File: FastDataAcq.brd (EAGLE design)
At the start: 160 x 100 mm, 229 parts, among them IC1 LT1963AEQ, IC2 FT230XQ, IC3 ADCMP553BRMZ, J1 USB_MICROAB_SMT, J2 MICRO-FIT_3.0_2POS_RA_SMD, X1 SMA-142-0701-801/806, X2 87832-14, X3 SMA-142-0701-801/806, Y1 SI530-500, Y2 DNP, Y3 100MHz

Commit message: Schematic fixes and beginning board layout
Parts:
- removed C105, C106, C107, C108, C109, C110, C111, C112: .1uF, Schuyler:0204REVERSE
- removed R40: 100 0.1%, rcl:R0402
- removed R41: 330, rcl:R0201
- added C16: .1uF, Schuyler:0204REVERSE
- added C66: 10pF, rcl:C0201
- added C67: 33uF, SparkFun-Passives:0805
- added C69, C73: 22uF 150mOhm ESR, rcl:C0805
- added C70, C72: 10uF, rcl:C0603
- added C75: NA, rcl:C0603
- C10, C11, C28, C29, C87: value 33uF -> .1uF; device SparkFun-Passives:0805 -> Schuyler:0204REVERSE
- C100: value .1uF -> 47pF; device Schuyler:0204REVERSE -> rcl:C0201
- C101, C103: value .1uF -> 10nF; device Schuyler:0204REVERSE -> rcl:C0201
- C102: value 4.7uF -> 1uF; device Schuyler:0306REVERSE -> Schuyler:0204REVERSE
- C12, C13, C15, C17, C22: value 10uF -> .1uF; device rcl:C0603 -> Schuyler:0204REVERSE
- C14, C25, C26, C27, C8, C9: value 10pF -> .1uF; device rcl:C0201 -> Schuyler:0204REVERSE
- C18: value NA -> 10uF
- C2: value 10uF -> 10pF; device rcl:C0603 -> rcl:C0201
- C20: value 10uF -> 100uF; device rcl:C0603 -> Schuyler:2917_MURATA_CAP
- C23, C24: value 22uF 150mOhm ESR -> .1uF; device rcl:C0805 -> Schuyler:0204REVERSE
- C3: value 100uF -> 33uF; device Schuyler:2917_MURATA_CAP -> SparkFun-Passives:0805
- C30, C38: value 33uF -> 0.47uF; device SparkFun-Passives:0805 -> Schuyler:0204REVERSE
- C31: value 22uF 150mOhm ESR -> 33uF; device rcl:C0805 -> SparkFun-Passives:0805
- C32, C65, C68: value 4.7uF -> 10uF; device Schuyler:0306REVERSE -> rcl:C0603
- C33, C71: value 4.7uF -> 10pF; device Schuyler:0306REVERSE -> rcl:C0201
- C34, C74: value 4.7uF -> 33uF; device Schuyler:0306REVERSE -> SparkFun-Passives:0805
- C35, C40, C50: device Schuyler:0306REVERSE -> Schuyler:0402_C
- C36, C37, C41, C42, C45, C62: value 0.47uF -> 4.7uF; device Schuyler:0306REVERSE -> Schuyler:0402_C
- C39: value 33uF -> 4.7uF; device SparkFun-Passives:0805 -> Schuyler:0402_C
- C43, C44, C47, C93: value .1uF -> 4.7uF; device Schuyler:0204REVERSE -> Schuyler:0402_C
- C46, C48, C49: value .1uF -> 0.47uF
- C5: value NA -> 10pF; device rcl:C0603 -> rcl:C0201
- C51, C52, C60: value 4.7uF -> 0.47uF; device Schuyler:0306REVERSE -> Schuyler:0204REVERSE
- C53, C58: value .1uF -> 10uF; device Schuyler:0204REVERSE -> rcl:C0603
- C54: value .1uF -> 10pF; device Schuyler:0204REVERSE -> rcl:C0201
- C55: value 0.47uF -> 33uF; device Schuyler:0306REVERSE -> SparkFun-Passives:0805
- C56: value 0.47uF -> 10uF; device Schuyler:0306REVERSE -> rcl:C0603
- C57: value 4.7uF -> 22uF 150mOhm ESR; device Schuyler:0306REVERSE -> rcl:C0805
- C59: value 10nF -> 4.7uF; device rcl:C0201 -> Schuyler:0402_C
- C6: value 10uF -> 33uF; device rcl:C0603 -> SparkFun-Passives:0805
- C61: device Schuyler:0306REVERSE -> Schuyler:0204REVERSE
- C63: value 1uF -> 0.47uF
- C64: value 10nF -> 0.47uF; device rcl:C0201 -> Schuyler:0204REVERSE
- C7: value 10uF -> NA
- C76: value 0.47uF -> 10nF; device Schuyler:0306REVERSE -> rcl:C0201
- C77: value 100pF -> .1uF; device rcl:C0603 -> Schuyler:0204REVERSE
- C78: value .1uF -> 1uF
- C79, C82: value .1uF -> 4.7nF; device Schuyler:0204REVERSE -> rcl:C0201
- C80: value 4.7nF -> .1uF; device rcl:C0201 -> Schuyler:0204REVERSE
- C81: value 4.7nF -> 1uF; device rcl:C0201 -> Schuyler:0204REVERSE
- C84: value 33uF -> 10nF; device SparkFun-Passives:0805 -> rcl:C0201
- C86: value 1uF -> 10nF; device Schuyler:0204REVERSE -> rcl:C0201
- C88: value 4.7uF -> 100pF; device Schuyler:0306REVERSE -> rcl:C0201
- C90, C94: value 10nF -> .1uF; device rcl:C0201 -> Schuyler:0204REVERSE
- C91: value .1uF -> 33uF; device Schuyler:0204REVERSE -> SparkFun-Passives:0805
- C92: value 10nF -> 4.7uF; device rcl:C0201 -> Schuyler:0306REVERSE
- C96: value 47pF -> .1uF; device rcl:C0201 -> Schuyler:0204REVERSE
- C98: value 47pF -> 33uF; device rcl:C0201 -> SparkFun-Passives:0805
- C99: value 1uF -> 47pF; device Schuyler:0204REVERSE -> rcl:C0201
- J1: value USB_MICROAB_SMT -> MICRO-FIT_3.0_2POS_RA_SMD; device Schuyler:USB_MICROAB_SMT_1 -> Schuyler:MICRO-FIT_3.02POS_RA_SMD
- J2: value MICRO-FIT_3.0_2POS_RA_SMD -> USB_MICROAB_SMT; device Schuyler:MICRO-FIT_3.02POS_RA_SMD -> Schuyler:USB_MICROAB_SMT_1
- JP2: value M10" -> (none); device SparkFun-Connectors:1X10 -> SparkFun-Passives:1X02
- JP3: value (none) -> M10"; device SparkFun-Passives:1X02 -> SparkFun-Connectors:1X10
- L10, L7, L9: value (none) -> 2.2uH; device Schuyler:MURATA_BLM18 -> Schuyler:3.0X3.6_VISHAY
- L12: value CHOKE_CM_ACM7060-301 -> (none); device Schuyler:ACM7060_CHOKE -> Schuyler:MURATA_BLM18
- L2: value 2.2uH -> CHOKE_CM_ACM7060-301; device Schuyler:3.0X3.6_VISHAY -> Schuyler:ACM7060_CHOKE
- L4, L5: value 2.2uH -> (none); device Schuyler:3.0X3.6_VISHAY -> Schuyler:MURATA_BLM18
- L6: value 2.2uH -> (none); device Schuyler:5.18X5.49_VISHAY -> Schuyler:MURATA_BLM18
- L8: value (none) -> 2.2uH; device Schuyler:MURATA_BLM18 -> Schuyler:5.18X5.49_VISHAY
- R1, R6: value NA -> 10k; device rcl:R0603 -> rcl:R0201
- R10: value NA -> 210K; device rcl:R0603 -> rcl:R0201
- R11: value 649K -> 422K
- R12: value 150K -> 10k
- R13: value NA -> 270k; device rcl:R0603 -> rcl:R0201
- R14: value 523K -> 1k
- R15: value 523K -> 845k
- R16: value 523K -> 210K
- R17: value 210K -> 270k
- R18: value 150K -> 523K
- R19: value 523K -> 806K
- R20: value 280K -> 649K
- R21: value 270k -> 523K
- R22: value 210K -> 1.15k 1%; device rcl:R0201 -> rcl:R0603
- R23, R34, R4, R8: value 10k -> NA; device rcl:R0201 -> rcl:R0603
- R24: value 1k -> 280K
- R25: value 210K -> 100; device rcl:R0201 -> rcl:R0603
- R26: value 806K -> 2k 1%; device rcl:R0201 -> rcl:R0603
- R27: value 845k -> 523K
- R28: value 649K -> NA; device rcl:R0201 -> rcl:R0603
- R29: value 422K -> 210K
- R30: value 270k -> 649K
- R31: value 1.15k 1% -> 523K; device rcl:R0603 -> rcl:R0201
- R32: value 2k 1% -> 150K; device rcl:R0603 -> rcl:R0201
- R33: value 50 -> 150K
- R35, R36: value 10k -> 100 0.1%; device rcl:R0201 -> rcl:R0402
- R37: value 10k -> 4.7k
- R38: value NA -> 330; device rcl:R0603 -> rcl:R0201
- R39: value 100 0.1% -> 0; device rcl:R0402 -> rcl:R0603
- R42: value 4.7k -> 330
- R43: value 0 -> 330; device rcl:R0603 -> rcl:R0201
- R46, R47: value 27 -> 330
- R48: value 10k -> 330; device rcl:R0603 -> rcl:R0201
- R49: value 26.1k -> 10k; device rcl:R0603 -> rcl:R0201
- R50: device rcl:R0603 -> rcl:R0201
- R51: value 16k -> 50; device rcl:R0603 -> rcl:R0201
- R52, R53: value 50 -> 27
- R54: value 50 -> 26.1k; device rcl:R0201 -> rcl:R0603
- R55: value 100 -> 16k
- R56, R57: value 330 -> 10k; device rcl:R0201 -> rcl:R0603
- R58: value 330 -> NA; device rcl:R0201 -> rcl:R0603
- R59, R60: value 330 -> 50
- R62: value NA -> 50; device rcl:R0603 -> rcl:R0201
- R7: value 3.3k 0.1% -> 4.7k; device rcl:R0603 -> rcl:R0201
- R9: value 4.7k -> 3.3k 0.1%; device rcl:R0201 -> rcl:R0603
- U$10: value XCFXXS04 -> LMH6555; device Schuyler:TSSOP20_XILINX -> Schuyler:16WQFN
- U$11: value SLIDER_SPDT_1101M2S3AQE2 -> LMV321SC-70; device Schuyler:C_AND_K_1101M2S3AQE2 -> Schuyler:SC-70
- U$3: value LTC3374QFN -> SLIDER_SPDT_1101M2S3AQE2; device Schuyler:38-QFN_(5X7) -> Schuyler:C_AND_K_1101M2S3AQE2
- U$4: value LT1963AEST-2.5 -> LTC3374QFN; device Schuyler:SOT223 -> Schuyler:38-QFN_(5X7)
- U$5: value LT1963AEST-3.3 -> LT1963AEST-2.5
- U$6: value TMP421 -> LT1963AEST-3.3; device Schuyler:SOT23-8 -> Schuyler:SOT223
- U$7: value LMH6555 -> XCFXXS04; device Schuyler:16WQFN -> Schuyler:TSSOP20_XILINX
- U$8: value LMV321SC-70 -> TMP421; device Schuyler:SC-70 -> Schuyler:SOT23-8
- X1: value SMA-142-0701-801/806 -> 87832-14; device con-coax:J502-ND-142-0701-801/806 -> con-molex:87832-14
- X2: value 87832-14 -> SMA-142-0701-801/806; device con-molex:87832-14 -> con-coax:J502-ND-142-0701-801/806
- Y2: value DNP -> 100MHz; device Schuyler:SI500S -> Schuyler:UMAX8
- Y3: value 100MHz -> DNP; device Schuyler:UMAX8 -> Schuyler:SI500S
- moved R59 1068.1 mm to (17.3, 26.4), turned to 90 degrees
- moved R57 1041.6 mm to (39.0, 12.0), flipped to the bottom, turned to 90 degrees
- moved R56 1034.7 mm to (30.0, 12.0), flipped to the bottom, turned to 90 degrees
- moved C59 999.3 mm to (99.5, 44.5), turned to 90 degrees
- moved C64 995.2 mm to (91.5, 38.1)
- moved C63 987.1 mm to (77.5, 38.1), turned to 180 degrees
- moved C44 968.7 mm to (85.5, 67.0)
- moved C43 967.8 mm to (85.5, 65.5)
- moved C46 955.8 mm to (98.0, 50.5), turned to 90 degrees
- moved C49 953.8 mm to (72.0, 53.2), turned to 90 degrees
- moved C48 953.0 mm to (72.0, 51.8), turned to 90 degrees
- moved C47 948.4 mm to (72.0, 46.5), turned to 90 degrees
- moved U$11 945.2 mm to (24.7, 59.0), turned to 180 degrees
- moved C104 941.8 mm to (27.0, 59.0), turned to 90 degrees
- moved X1 913.6 mm to (107.4, 70.8), turned to 90 degrees
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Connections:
- removed net 1V9F: C33.P$1, C36.P$1, C41.P$1, C50.P$1, C51.P$1, C55.P$1, C56.P$1, C61.P$1, C62.P$1
- removed net VCCAUX: U$2.P$20
- removed net VCCINT: U$2.P$19, U$2.P$28
- net !RXLED: now also D5.CATHODE; no longer D2.CATHODE
- net !TXLED: now also D6.CATHODE; no longer D3.CATHODE
- net 1V2: now also C2.1, C3.1, C36.P$1, C37.P$1, C38.P$1, L1.P$2, R10.2, R13.1, TP1.TP, U$2.P$19, U$2.P$28; no longer C25.1, C28.1, C32.P$1, C40.P$1, C45.P$1, L4.P$2, R21.1, R25.2, TP2.TP
- net 1V8: now also C33.1, C34.1, C47.P$1, C48.P$1, C49.P$1, C50.P$1, C51.P$1, C52.P$1, C62.P$1, C63.P$1, C64.P$1, L7.P$2, R19.2, TP5.TP; no longer C26.1, C29.1, L5.P$2, R26.2, TP4.TP, U$2.P$77
- net 1V9: now also C57.1, L4.P$1, L6.P$1, R22.2, R25.2; no longer C31.1, L7.P$1, L8.P$1, R31.2, R55.2
- net 1V9A: now also C10.P$2, C11.P$1, C12.P$1, C13.P$2, C14.P$1, C15.P$1, C16.P$2, C17.P$1, C19.1, C8.P$1, C9.P$2, L4.P$2, R2.2, R6.1; no longer C103.P$1, C104.P$1, C105.P$1, C106.P$1, C107.P$1, C108.P$1, C109.P$1, C110.P$1, C111.P$1, C112.P$1, C38.1, L7.P$2, R4.1, R6.2
- net 1V9D: now also C22.P$1, C23.P$1, C24.P$1, C25.P$1, C26.P$1, C27.P$1, C28.P$1, C29.P$1, C30.P$1, C31.1, L6.P$2; no longer C39.1, C43.P$1, C44.P$1, C46.P$1, C47.P$1, C48.P$1, C49.P$1, C53.P$1, C54.P$1, C58.P$1, L8.P$2
- net 2V3_1V9PRE: now also C54.1, C55.1, C56.1, L8.P$2, R21.2, TP6.TP; no longer C14.1, C19.1, C22.1, L3.P$2, R19.2, TP3.TP
- net 2V5: now also C69.1, L11.P$2, TP9.TP, U$5.3; no longer C23.1, L10.P$2, TP8.TP, U$4.3
- net 2V5A: now also C76.1, C77.P$1, C78.P$1, L11.P$1; no longer C64.1, C85.P$1, C86.P$1, L10.P$1
- net 2V8_2V5PRE: now also C66.1, C67.1, C68.1, L9.P$2, R27.2, R30.1, TP8.TP, U$5.1; no longer C10.1, C20.1, C8.1, L1.P$2, R11.1, R15.2, TP1.TP, U$4.1
- net 3V3: now also C102.P$1, C103.1, C39.P$1, C40.P$1, C41.P$1, C43.P$1, C44.P$1, C45.P$1, C46.P$1, C5.1, C59.P$1, C6.1, C61.P$1, C80.P$1, C81.P$1, C84.1, C85.P$1, C86.1, C87.P$1, C94.P$1, C95.1, C98.1, JP3.10, L3.P$2, R15.2, R34.2, R42.1, R43.1, R44.1, R49.2, R50.2, R7.2, TP3.TP, U$2.P$20, U$7.P$18, U$7.P$19, U$7.P$20, U$8.P$8, X1.2, Y2.P$2, Y2.P$3, Y2.P$6, Y3.P$1, Y3.P$4; no longer C27.1, C30.1, C34.P$1, C37.P$1, C52.P$1, C57.P$1, C59.1, C63.P$1, C65.P$1, C68.P$1, C71.P$1, C74.P$1, C76.P$1, C87.1, C88.P$1, C89.P$1, C90.1, C91.P$1, C92.1, C94.1, C97.P$1, C99.P$1, JP2.10, L6.P$2, R27.2, R36.2, R37.2, R39.2, R41.2, R58.1, R59.1, R60.1, R9.2, TP6.TP, U$10.P$18, U$10.P$19, U$10.P$20, U$6.P$8, X2.2, Y2.P$1, Y2.P$4, Y3.P$2, Y3.P$3, Y3.P$6
- net 3V3A: now also C73.1, L12.P$2, TP10.TP, U$6.3; no longer C24.1, L9.P$2, TP9.TP, U$5.3
- net 3V3S: now also C104.P$1, C89.P$1, C90.P$1, C91.1, L12.P$1, U$10.P$11, U$10.P$12, U$10.P$9, U$11.P$5; no longer C78.P$1, C79.P$1, C82.P$1, C84.1, L9.P$1, U$7.P$11, U$7.P$12, U$7.P$9, U$8.P$5
- net 3V6_PRE3V3: now also C71.1, C72.1, C74.1, L10.P$2, R31.2, TP11.TP, U$6.1; no longer C11.1, C21.1, C9.1, L2.P$2, R16.2, TP5.TP, U$5.1
- net 5VUSB: now also C92.P$1, C97.P$2, L13.P$2; no longer C101.P$2, C102.P$1, L11.P$2
- net 5VUSB_CON: now also C101.1, J2.VCC, L13.P$1; no longer C95.1, J1.VCC, L11.P$1
- net ADC_CAL: now also R6.2; no longer R5.2
- net ADC_CALDLY/DES/!SCS: now also R1.1; no longer R8.1
- net ADC_CLK+: now also C79.2; no longer C80.2
- net ADC_CLK-: now also C82.2; no longer C81.2
- net ADC_DCLKRST: now also R4.2; no longer R3.2
- net ADC_FSR/ECE: now also R2.1, R3.2; no longer R1.1, R2.2
- net ADC_PD: now also R5.2; no longer R4.2
- net ADC_PWR_EN: now also R23.2, U$4.P$19; no longer R13.2, U$3.P$19
- net ADC_REXT: now also R9.2; no longer R7.2
- net ADC_TDIODE+: now also C88.1, U$8.P$1; no longer C77.1, U$6.P$1
- net ADC_TDIODE-: now also C88.2, U$8.P$2; no longer C77.2, U$6.P$2
- net ADC_VBG: now also R8.1; no longer R6.1
- net ADC_VCMO: now also U$11.P$1; no longer U$8.P$1
- net ADC_VCMO_BUFFER: now also U$10.P$10, U$11.P$3, U$11.P$4; no longer U$7.P$10, U$8.P$3, U$8.P$4
- net ADC_VINI+: now also U$10.P$8; no longer U$7.P$8
- net ADC_VINI-: now also U$10.P$13; no longer U$7.P$13
- net AGND: now also C10.P$1, C11.P$2, C12.P$2, C13.P$1, C14.P$2, C15.P$2, C16.P$1, C17.P$2, C19.2, C76.2, C77.P$2, C8.P$2, C89.P$2, C9.P$1, C90.P$2, C91.2, R4.1, R51.1, R9.1, U$10.P$1, U$10.P$14, U$10.P$15, U$10.P$17, U$10.P$2, U$10.P$3, U$10.P$4, U$10.P$6, U$10.P$7, U$11.P$2, X2.G@1, X2.G@2, X2.G@3, X2.G@4; no longer C103.P$2, C105.P$2, C106.P$2, C107.P$2, C108.P$2, C109.P$2, C110.P$2, C111.P$2, C112.P$2, C38.2, C64.2, C79.P$2, C82.P$2, C84.2, C85.P$2, C86.P$2, R2.1, R33.1, R7.1, U$7.P$1, U$7.P$14, U$7.P$15, U$7.P$17, U$7.P$2, U$7.P$3, U$7.P$4, U$7.P$6, U$7.P$7, U$8.P$2, X3.G@1, X3.G@2, X3.G@3, X3.G@4
- net ANALOG_PWR_EN: now also R28.2, U$4.P$32; no longer R10.2, U$3.P$32
- net CLK500+: now also C82.1; no longer C81.1
- net CLK500-: now also C79.1; no longer C80.1
- net DGND: now also C100.1, C101.2, C103.2, C20.P$1, C22.P$2, C23.P$2, C24.P$2, C25.P$2, C26.P$2, C27.P$2, C28.P$2, C29.P$2, C3.2, C32.2, C34.2, C38.P$2, C39.P$2, C53.2, C55.2, C56.2, C57.2, C58.2, C59.P$2, C64.P$2, C65.2, C67.2, C68.2, C69.2, C70.2, C72.2, C73.2, C74.2, C75.2, C80.P$2, C81.P$2, C84.2, C85.P$2, C86.2, C87.P$2, C92.P$2, C94.P$2, C96.P$1, C97.P$1, C98.2, C99.1, J2.GND, JP3.9, L2.P$3, R11.1, R16.1, R23.1, R24.1, R25.1, R26.1, R32.2, R33.1, R36.1, R58.2, R59.1, R62.1, U$2.P$77, U$2.P$91, U$4.P$16, U$4.P$18, U$4.P$37, U$4.P$39, U$6.2, U$6.4, U$7.P$11, U$8.P$3, U$8.P$4, U$8.P$5, X1.1, X1.11, X1.13, X1.3, X1.5, X1.7, X1.9, X3.G@1, X3.G@2, X3.G@3, X3.G@4, Y2.P$4, Y2.P$5, Y3.P$2; no longer C10.2, C100.P$1, C101.P$1, C11.2, C12.2, C13.2, C15.2, C17.2, C19.2, C2.2, C20.2, C22.2, C23.2, C24.2, C28.2, C29.2, C3.P$1, C30.2, C32.P$2, C33.P$2, C34.P$2, C39.2, C5.2, C53.P$2, C54.P$2, C55.P$2, C56.P$2, C57.P$2, C58.P$2, C59.2, C65.P$2, C68.P$2, C71.P$2, C74.P$2, C76.P$2, C87.2, C88.P$2, C89.P$2, C90.2, C91.P$2, C92.2, C94.2, C96.1, C97.P$2, C98.1, C99.P$2, J1.GND, JP2.9, L12.P$3, R10.1, R12.2, R13.1, R14.1, R22.1, R30.1, R32.1, R40.1, R54.1, R55.1, R61.1, R62.2, U$10.P$11, U$3.P$16, U$3.P$18, U$3.P$37, U$3.P$39, U$4.2, U$4.4, U$6.P$3, U$6.P$4, U$6.P$5, X1.G@1, X1.G@2, X1.G@3, X1.G@4, X2.1, X2.11, X2.13, X2.3, X2.5, X2.7, X2.9, Y2.P$2, Y3.P$4, Y3.P$5
- net FPGA_CCLK: now also R34.1, R35.1, R36.2, U$7.P$3; no longer R38.1, R39.1, R40.2, U$10.P$3
- net FPGA_CLK1: now also Y2.P$1; no longer Y3.P$1
- net FPGA_CLK2: now also Y3.P$3; no longer Y2.P$3
- net FPGA_DIN: now also U$7.P$1; no longer U$10.P$1
- net FPGA_DONE: now also R38.1, TP13.TP, U$7.P$10; no longer R41.1, TP12.TP, U$10.P$10
- net FPGA_GPIO0: now also JP3.1; no longer JP2.1
- net FPGA_GPIO1: now also JP3.2; no longer JP2.2
- net FPGA_GPIO2: now also JP3.3; no longer JP2.3
- net FPGA_GPIO3: now also JP3.4; no longer JP2.4
- net FPGA_GPIO4: now also JP3.5; no longer JP2.5
- net FPGA_GPIO5: now also D4.CATHODE, JP3.6; no longer D6.CATHODE, JP2.6
- net FPGA_GPIO6: now also D3.CATHODE, JP3.7; no longer D5.CATHODE, JP2.7
- net FPGA_GPIO7: now also D2.CATHODE, JP3.8; no longer D4.CATHODE, JP2.8
- net FPGA_INITB: now also TP12.TP, U$7.P$8; no longer TP13.TP, U$10.P$8
- net FPGA_PROGRAMB: now also R39.2, R7.1; no longer R43.2, R9.1
- net FPGA_RXD: now also R47.2; no longer R44.2
- net FPGA_SCL: now also R50.1, U$8.P$7; no longer R36.1, U$6.P$7
- net FPGA_SDA: now also R49.1, U$8.P$6; no longer R35.1, R37.1, U$6.P$6
- net FPGA_TCK: now also U$7.P$6, X1.6; no longer U$10.P$6, X2.6
- net FPGA_TDI: now also X1.10; no longer X2.10
- net FPGA_TDO: now also U$7.P$4; no longer U$10.P$4
- net FPGA_TMS: now also U$7.P$5, X1.4; no longer U$10.P$5, X2.4
- net FPGA_TRIG+: now also R57.2, R61.2; no longer R48.2, R53.2
- net FPGA_TRIG-: now also R56.2, R60.2; no longer R50.2, R52.2
- net FPGA_TXD: now also R48.2; no longer R45.2
- net FTDI_RXD: now also R48.1; no longer R45.1
- net FTDI_TXD: now also R47.1; no longer R44.1
- net N$1: now also JP1.2, L2.P$4, U$3.P$1; no longer JP3.2, L12.P$4, U$11.P$1
- net N$10: now also D5.ANODE, R45.2; no longer D2.ANODE, R56.2
- net N$11: now also R39.1, U$7.P$7; no longer R43.1, U$10.P$7
- net N$12: now also C7.1, R13.2, R16.2, U$4.P$38; no longer C18.1, R21.2, R22.2, U$3.P$38
- net N$13: now also D6.ANODE, R46.2; no longer D3.ANODE, R57.2
- net N$14: now also R22.1, R26.2; no longer R31.1, R32.2
- net N$15: now also R54.2, R57.1; no longer R48.1, R49.2
- net N$16: now also C75.1, R30.2, R32.1, U$4.P$14; no longer C5.1, R11.2, R12.1, U$3.P$14
- net N$17: now also C20.P$2, JP1.1, L5.P$1, R14.2, U$3.P$2; no longer C3.P$2, JP3.1, L13.P$1, R24.2, U$11.P$2
- net N$18: now also R60.1, R61.1, R62.2; no longer R52.1, R53.1, R54.2
- net N$19: now also D4.ANODE, R44.2; no longer D6.ANODE, R60.2
- net N$2: now also R51.2, U$10.P$5; no longer R33.2, U$7.P$5
- net N$20: now also R55.2, R56.1; no longer R50.1, R51.2
- net N$21: now also D3.ANODE, R43.2; no longer D5.ANODE, R59.2
- net N$22: now also D2.ANODE, R42.2; no longer D4.ANODE, R58.2
- net N$26: no longer U$2.P$91
- net N$3: now also R52.2; no longer R46.2
- net N$4: now also C99.2, J2.D+, R52.1; no longer C96.2, J1.D+, R46.1
- net N$5: now also C100.2, J2.D-, R53.1; no longer C98.2, J1.D-, R47.1
- net N$6: now also JP2.1, R18.2, U$4.P$34; no longer JP1.1, R14.2, U$3.P$34
- net N$7: now also R53.2; no longer R47.2
- net N$8: now also C96.P$2, R45.1, R46.1; no longer C100.P$2, R56.1, R57.1
- net N$9: now also R14.1; no longer R24.1
- net PGOOD: now also R12.1, TP2.TP, U$4.P$15; no longer R23.1, TP11.TP, U$3.P$15
- net POWER_IN+: now also J1.P$2, L2.P$1; no longer J2.P$2, L12.P$1
- net POWER_IN-: now also J1.P$1, L2.P$2; no longer J2.P$1, L12.P$2
- net PROM_TDO: now also U$7.P$17, X1.8; no longer U$10.P$17, X2.8
- net S1FB: now also C5.2, R15.1, R17.2, U$4.P$1; no longer C27.2, R27.1, R30.2, U$3.P$1
- net S1SW: now also L3.P$1, U$4.P$3, U$4.P$4; no longer L6.P$1, U$3.P$3, U$3.P$4
- net S3FB: now also C71.2, R31.1, R33.2, U$4.P$7; no longer C9.2, R16.1, R18.2, U$3.P$7
- net S3SW: now also L10.P$1, U$4.P$9; no longer L2.P$1, U$3.P$9
- net S4FB: now also C33.2, R19.1, R20.2, U$4.P$12; no longer C26.2, R26.1, R28.2, U$3.P$12
- net S4SW: now also L7.P$1, U$4.P$10; no longer L5.P$1, U$3.P$10
- net S5FB: now also C54.2, R21.1, R24.2, U$4.P$20; no longer C14.2, R19.1, R20.2, U$3.P$20
- net S5SW: now also L8.P$1, U$4.P$22, U$4.P$23; no longer L3.P$1, U$3.P$22, U$3.P$23
- net S7FB: now also C2.2, R10.1, R11.2, U$4.P$26; no longer C25.2, R25.1, R29.2, U$3.P$26
- net S7SW: now also L1.P$1, U$4.P$28; no longer L4.P$1, U$3.P$28
- net S8FB: now also C66.2, R27.1, R29.2, U$4.P$31; no longer C8.2, R15.1, R17.2, U$3.P$31
- net S8SW: now also L9.P$1, U$4.P$29; no longer L1.P$1, U$3.P$29
- net SIGNAL_IN: now also U$10.P$16, X2.1; no longer U$7.P$16, X3.1
- net S_TEMP: now also TP4.TP, U$4.P$36; no longer TP10.TP, U$3.P$36
- net TRIGGER: now also R59.2, X3.1; no longer R61.2, X1.1
- net TRIG_REF: now also R58.1; no longer R62.1
- net TRIG_RESET_HIGH: now also R55.1; no longer R51.1
- net TRIG_RESET_LOW: now also R54.1; no longer R49.1
- net VCC: now also JP2.2; no longer JP1.2
- net VIN: now also C18.1, C21.1, C32.1, C53.1, C58.1, C65.1, C70.1, L5.P$2, U$4.P$11, U$4.P$13, U$4.P$17, U$4.P$2, U$4.P$21, U$4.P$24, U$4.P$25, U$4.P$27, U$4.P$30, U$4.P$33, U$4.P$35, U$4.P$5, U$4.P$6, U$4.P$8; no longer C12.1, C13.1, C15.1, C17.1, C2.1, C6.1, C7.1, L13.P$2, U$3.P$11, U$3.P$13, U$3.P$17, U$3.P$2, U$3.P$21, U$3.P$24, U$3.P$25, U$3.P$27, U$3.P$30, U$3.P$33, U$3.P$35, U$3.P$5, U$3.P$6, U$3.P$8
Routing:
- net DQ2-: track 77.5 -> 93.5 mm
- net DQ1-: track 75.8 -> 91.8 mm
- net DQ2+: track 77.8 -> 93.8 mm
- net DQD6-: track 75.1 -> 91.0 mm
- net DQ1+: track 76.5 -> 92.4 mm
- net DQD6+: track 75.7 -> 91.6 mm
- net DQD7-: track 75.5 -> 91.3 mm
- net DQD7+: track 76.1 -> 91.8 mm
- net DQ0-: track 75.8 -> 91.6 mm
- net DQ0+: track 76.4 -> 92.1 mm
- net DQD5-: track 77.0 -> 90.2 mm
- net DQD5+: track 77.6 -> 90.7 mm
- net DQD4-: track 78.5 -> 90.2 mm
- net DQD4+: track 79.1 -> 90.7 mm
- net DID6-: track 75.1 -> 85.3 mm
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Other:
- board text added: "Check footprint for IC3"

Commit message: Board layout in progress. Other minor fixes.
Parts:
- removed C30: 0.47uF, Schuyler:0204REVERSE
- moved R58 1183.1 mm to (107.9, 97.9), turned to 90 degrees
- moved R46 1107.7 mm to (145.2, 47.5)
- moved R14 1105.9 mm to (138.2, 59.4), turned to 270 degrees
- moved D1 1104.0 mm to (138.3, 61.3), turned to 270 degrees
- moved R45 1101.5 mm to (145.2, 45.7)
- moved D6 1100.2 mm to (147.1, 47.5), turned to 180 degrees
- moved D5 1097.7 mm to (147.1, 45.7), turned to 180 degrees
- moved JP1 1095.9 mm to (143.0, 59.2), turned to 90 degrees
- moved R44 1094.3 mm to (144.8, 9.14), turned to 270 degrees
- moved R43 1090.6 mm to (146.8, 9.14), turned to 270 degrees
- moved R42 1086.8 mm to (148.6, 9.14), turned to 270 degrees
- moved JP3 1075.1 mm to (150.2, 2.24), turned to 180 degrees
- moved D4 1073.2 mm to (144.8, 7.11), turned to 90 degrees
- moved H3 1073.1 mm to (9.32, 96.2), turned to 90 degrees
- moved D3 1073.0 mm to (146.8, 7.11), turned to 90 degrees
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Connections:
- removed net VCC: JP2.2
- net 1V9D: no longer C30.P$1
- net 3V3: now also R12.2, R37.2
- net FPGA_INITB: now also R37.1
- net VIN: now also JP2.2

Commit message: Minor schematic fixes, major PCB layout changes
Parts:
- removed R58: NA, rcl:R0603
- D1, D4: value (none) -> LED_0603_RED
- D2, D6: value (none) -> LED_0603_BLUE
- D3, D5: value (none) -> LED_0603_GREEN
- JP1, JP2: value (none) -> JUMPER-2PTH
- L11, L12, L4, L5, L6: value (none) -> 26
- L13: value (none) -> 330
- moved H1 150.8 mm to (5.00, 76.3)
- moved R54 101.5 mm to (137.3, 6.16)
- moved R55 101.5 mm to (134.3, 6.16)
- moved R56 101.5 mm to (131.3, 6.16)
- moved R57 101.5 mm to (140.3, 6.16)
- moved L2 73.8 mm to (97.4, 11.5), turned to 0 degrees
- moved C3 56.5 mm to (100.8, 64.6), flipped to the bottom, turned to 180 degrees
- moved IC1 56.5 mm to (75.2, 72.3), turned to 90 degrees
- moved L1 54.5 mm to (96.2, 63.3), flipped to the bottom, turned to 90 degrees
- moved C55 50.1 mm to (83.7, 60.5), flipped to the bottom, turned to 90 degrees
- moved C67 50.1 mm to (102.7, 60.5), flipped to the bottom, turned to 90 degrees
- moved J1 49.5 mm to (109.1, 50.4)
- moved JP1 49.4 mm to (105.4, 27.2)
- moved D1 49.4 mm to (100.7, 29.3)
- moved U$3 49.4 mm to (114.4, 26.0)
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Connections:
- net N$8 renamed 3V3OUT
- removed net AGND: C10.P$1, C104.P$2, C11.P$2, C12.P$2, C13.P$1, C14.P$2, C15.P$2, C16.P$1, C17.P$2, C19.2, C76.2, C77.P$2, C78.P$2, C8.P$2, C89.P$2, C9.P$1, C90.P$2, C91.2, R3.1, R4.1, R51.1, R9.1, U$1.P$1, U$1.P$12, U$1.P$129, U$1.P$21, U$1.P$24, U$1.P$27, U$1.P$41, U$1.P$6, U$1.P$9, U$10.P$1, U$10.P$14, U$10.P$15, U$10.P$17, U$10.P$2, U$10.P$3, U$10.P$4, U$10.P$6, U$10.P$7, U$11.P$2, X2.G@1, X2.G@2, X2.G@3, X2.G@4, Y1.P$3
- removed net DGND: C1.2, C100.1, C101.2, C102.P$2, C103.2, C18.2, C20.P$1, C21.2, C22.P$2, C23.P$2, C24.P$2, C25.P$2, C26.P$2, C27.P$2, C28.P$2, C29.P$2, C3.2, C31.2, C32.2, C34.2, C35.P$2, C36.P$2, C37.P$2, C38.P$2, C39.P$2, C4.2, C40.P$2, C41.P$2, C42.P$2, C43.P$2, C44.P$2, C45.P$2, C46.P$2, C47.P$2, C48.P$2, C49.P$2, C50.P$2, C51.P$2, C52.P$2, C53.2, C55.2, C56.2, C57.2, C58.2, C59.P$2, C6.2, C60.P$2, C61.P$2, C62.P$2, C63.P$2, C64.P$2, C65.2, C67.2, C68.2, C69.2, C7.2, C70.2, C72.2, C73.2, C74.2, C75.2, C80.P$2, C81.P$2, C83.P$2, C84.2, C85.P$2, C86.2, C87.P$2, C92.P$2, C93.P$2, C94.P$2, C95.2, C96.P$1, C97.P$1, C98.2, C99.1, D1.CATHODE, IC1.3, IC1.6, IC2.3, IC3.8, J2.GND, JP3.9, L2.P$3, R11.1, R16.1, R17.1, R18.1, R20.1, R23.1, R24.1, R25.1, R26.1, R28.1, R29.1, R32.2, R33.1, R36.1, R58.2, R59.1, R62.1, U$1.P$108, U$1.P$119, U$1.P$42, U$1.P$53, U$1.P$64, U$1.P$74, U$1.P$87, U$1.P$97, U$2.P$113, U$2.P$13, U$2.P$130, U$2.P$136, U$2.P$25, U$2.P$3, U$2.P$49, U$2.P$54, U$2.P$60, U$2.P$68, U$2.P$73, U$2.P$77, U$2.P$91, U$4.P$16, U$4.P$18, U$4.P$37, U$4.P$39, U$5.2, U$5.4, U$6.2, U$6.4, U$7.P$11, U$8.P$3, U$8.P$4, U$8.P$5, U$9.P$3, U$9.P$6, X1.1, X1.11, X1.13, X1.3, X1.5, X1.7, X1.9, X3.G@1, X3.G@2, X3.G@3, X3.G@4, Y2.P$4, Y2.P$5, Y3.P$2
- removed net FPGA_GPIO0: JP3.1, U$2.P$46
- removed net FPGA_SDL: U$2.P$44
- removed net N$26: U$2.P$108, U$2.P$96
- net 1V8: now also R12.2
- net 3V3: no longer R12.2
- net FPGA_SDA: now also U$2.P$44
- net GND: now also C1.2, C10.P$1, C100.1, C101.2, C102.P$2, C103.2, C104.P$2, C11.P$2, C12.P$2, C13.P$1, C14.P$2, C15.P$2, C16.P$1, C17.P$2, C18.2, C19.2, C20.P$1, C21.2, C22.P$2, C23.P$2, C24.P$2, C25.P$2, C26.P$2, C27.P$2, C28.P$2, C29.P$2, C3.2, C31.2, C32.2, C34.2, C35.P$2, C36.P$2, C37.P$2, C38.P$2, C39.P$2, C4.2, C40.P$2, C41.P$2, C42.P$2, C43.P$2, C44.P$2, C45.P$2, C46.P$2, C47.P$2, C48.P$2, C49.P$2, C50.P$2, C51.P$2, C52.P$2, C53.2, C55.2, C56.2, C57.2, C58.2, C59.P$2, C6.2, C60.P$2, C61.P$2, C62.P$2, C63.P$2, C64.P$2, C65.2, C67.2, C68.2, C69.2, C7.2, C70.2, C72.2, C73.2, C74.2, C75.2, C76.2, C77.P$2, C78.P$2, C8.P$2, C80.P$2, C81.P$2, C83.P$2, C84.2, C85.P$2, C86.2, C87.P$2, C89.P$2, C9.P$1, C90.P$2, C91.2, C92.P$2, C93.P$2, C94.P$2, C95.2, C96.P$1, C97.P$1, C98.2, C99.1, D1.CATHODE, IC1.3, IC1.6, IC2.3, IC3.8, J2.GND, JP3.9, L2.P$3, R11.1, R16.1, R17.1, R18.1, R20.1, R23.1, R24.1, R25.1, R26.1, R28.1, R29.1, R3.1, R32.2, R33.1, R36.1, R4.1, R51.1, R59.1, R62.1, R9.1, U$1.P$1, U$1.P$108, U$1.P$119, U$1.P$12, U$1.P$129, U$1.P$21, U$1.P$24, U$1.P$27, U$1.P$41, U$1.P$42, U$1.P$53, U$1.P$6, U$1.P$64, U$1.P$74, U$1.P$87, U$1.P$9, U$1.P$97, U$10.P$1, U$10.P$14, U$10.P$15, U$10.P$17, U$10.P$2, U$10.P$3, U$10.P$4, U$10.P$6, U$10.P$7, U$11.P$2, U$2.P$108, U$2.P$113, U$2.P$13, U$2.P$130, U$2.P$136, U$2.P$25, U$2.P$3, U$2.P$49, U$2.P$54, U$2.P$60, U$2.P$68, U$2.P$73, U$2.P$77, U$2.P$91, U$2.P$96, U$4.P$16, U$4.P$18, U$4.P$37, U$4.P$39, U$5.2, U$5.4, U$6.2, U$6.4, U$7.P$11, U$8.P$3, U$8.P$4, U$8.P$5, U$9.P$3, U$9.P$6, X1.1, X1.11, X1.13, X1.3, X1.5, X1.7, X1.9, X2.G@1, X2.G@2, X2.G@3, X2.G@4, X3.G@1, X3.G@2, X3.G@3, X3.G@4, Y1.P$3, Y2.P$4, Y2.P$5, Y3.P$2
- net PGOOD: now also U$2.P$35; no longer U$2.P$45
- net TRIG_REF: no longer R58.1
- net TRIG_RESET_HIGH: now also U$2.P$46
- net TRIG_RESET_LOW: now also U$2.P$45
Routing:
- net DID6+: track 85.9 -> 68.7 mm
- net DID6-: track 85.3 -> 68.2 mm
- net DI0+: track 86.4 -> 69.2 mm
- net DI0-: track 85.9 -> 68.7 mm
- net DID7-: track 85.6 -> 68.4 mm
- net DID7+: track 86.1 -> 69.0 mm
- net DI1+: track 85.0 -> 68.0 mm
- net DI1-: track 85.3 -> 68.4 mm
- net DID5-: track 84.5 -> 67.6 mm
- net DID5+: track 85.1 -> 68.1 mm
- net DID2+: track 88.8 -> 72.5 mm
- net DID2-: track 88.3 -> 72.0 mm
- net DID3-: track 86.7 -> 70.6 mm
- net DID3+: track 87.2 -> 71.1 mm
- net DID4-: track 84.8 -> 68.7 mm
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
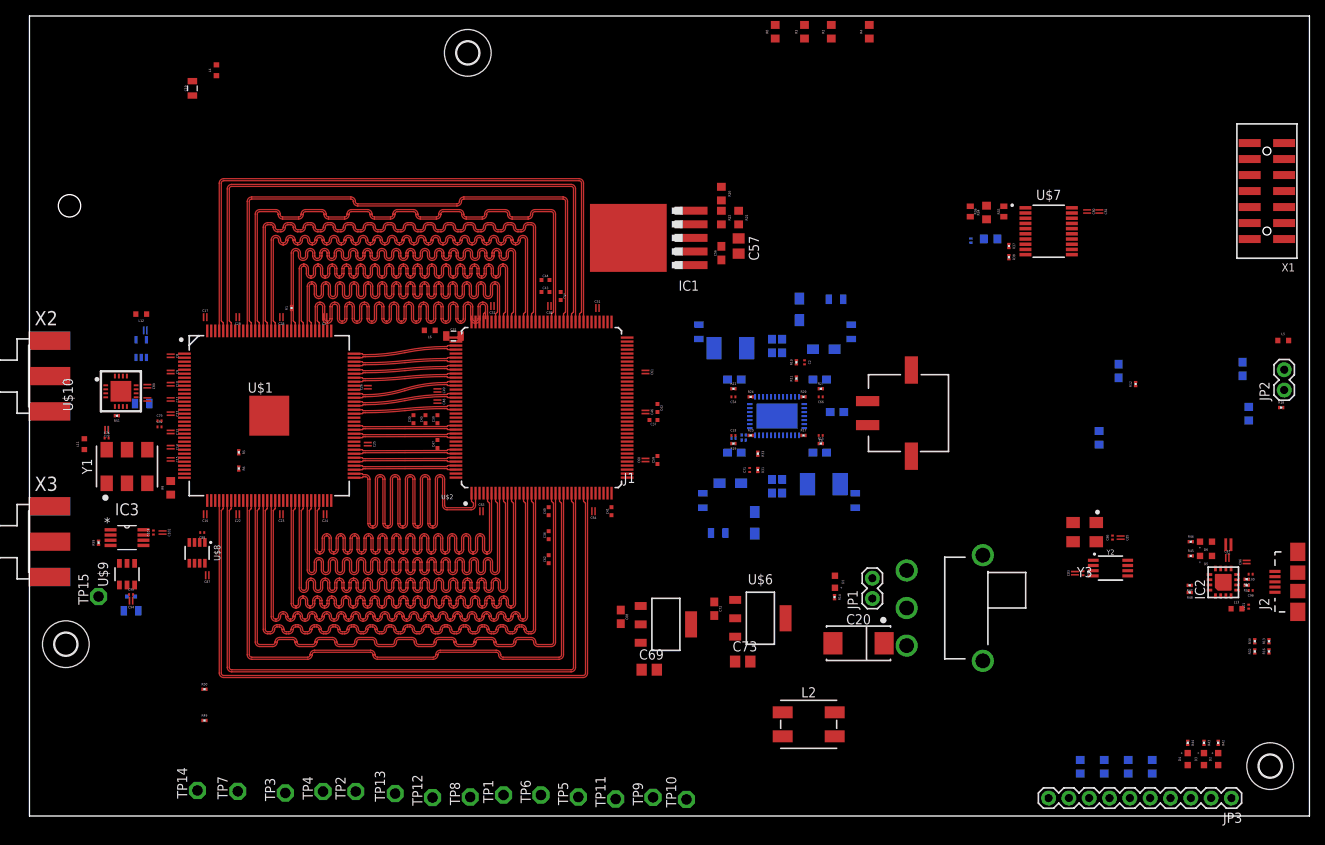
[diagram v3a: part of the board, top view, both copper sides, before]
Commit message: Now includes python layout scripts
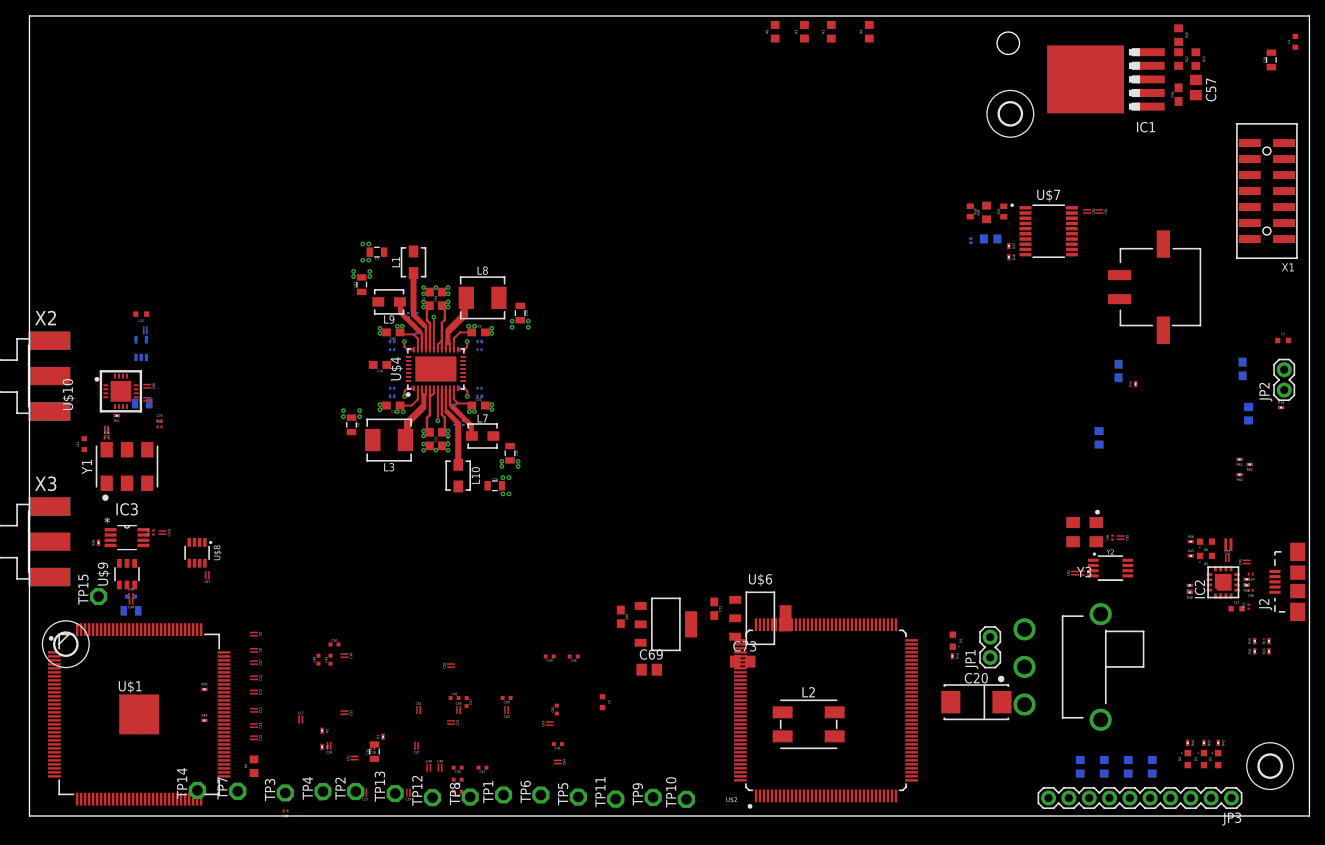
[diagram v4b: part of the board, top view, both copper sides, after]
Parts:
- moved C19 134.9 mm to (155.2, 94.5)
- moved L4 134.9 mm to (158.2, 96.8)
- moved H1 119.1 mm to (122.4, 96.6)
- moved H3 68.2 mm to (122.6, 87.8)
- moved R62 64.6 mm to (152.5, 43.9), flipped to the top
- moved C51 63.9 mm to (40.6, 7.25), turned to 270 degrees
- moved C6 63.7 mm to (40.3, 48.9), flipped to the top
- moved R60 62.1 mm to (151.3, 42.7), flipped to the top
- moved R61 62.1 mm to (151.3, 44.6), flipped to the top
- moved C67 61.5 mm to (41.5, 66.4), flipped to the top
- moved C56 60.5 mm to (143.6, 90.2)
- moved IC1 60.5 mm to (132.3, 92.1)
- moved R22 60.5 mm to (143.6, 94.6)
- moved R26 60.5 mm to (143.6, 97.6)
- moved C57 60.5 mm to (145.8, 91.1)
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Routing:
- net DQD0+: track 90.6 -> 0.00 mm
- net DQD0-: track 90.0 -> 0.00 mm
- net DQD1+: track 86.6 -> 0.00 mm
- net DQD1-: track 86.1 -> 0.00 mm
- net DID0+: track 81.8 -> 0.00 mm
- net DID0-: track 81.3 -> 0.00 mm
- net DQD2+: track 80.9 -> 0.00 mm
- net DQD2-: track 80.4 -> 0.00 mm
- net DQ2+: track 79.7 -> 0.00 mm
- net DQD3+: track 79.6 -> 0.00 mm
- net DQ2-: track 79.4 -> 0.00 mm
- net DQD3-: track 79.1 -> 0.00 mm
- net DID1+: track 78.4 -> 0.00 mm
- net DQ1+: track 78.2 -> 0.00 mm
- net DQ0+: track 78.0 -> 0.00 mm
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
